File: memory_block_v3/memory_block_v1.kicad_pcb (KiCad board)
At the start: 4 copper layers, 69.6 x 49.6 mm, 15 parts, among them J1 4677, J11 Conn_01x07, J2 DM3D-SF, J3 Conn_01x02, J4 Conn_01x19, J5 Conn_01x03, J6 Conn_01x19, J7 PinSocket_1x03_P2.54mm_Vertic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, U1 ESP32-WROOM-32E-N4, U2 W25Q128JVSIQ TR

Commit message: Start of NB/MB PCB Rework
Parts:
- removed J7: PinSocket_1x03_P2.54mm_Vertical, Connector_PinSocket_2.54mm:PinSocket_1x03_P2.54mm_Vertical
- added C1: 10 uF, Capacitor_THT:CP_Radial_D10.0mm_P2.50mm, F.Cu at (342.1, 304.6)
- added C2: 0.1uF, Capacitor_THT:C_Rect_L7.5mm_W6.5mm_P5.00mm, F.Cu at (345.2, 292.9)
- added D1: LED, LED_THT:LED_D3.0mm, F.Cu at (337.8, 296.2)
- added R1: 220 Ω, Resistor_THT:R_Axial_DIN0207_L6.3mm_D2.5mm_P7.62mm_Horizontal, F.Cu at (337.8, 280.4)
- added R2: 10 kΩ, Resistor_THT:R_Axial_DIN0207_L6.3mm_D2.5mm_P7.62mm_Horizontal, F.Cu at (345.2, 280.4)
- U1: value ESP32-WROOM-32E-N4 -> ESP32-WROOM-32E-N8
- moved J5 90.1 mm to (378.7, 320.5)
- moved J11 82.4 mm to (378.7, 299.7)
- moved U1 54.8 mm to (362.2, 307.2)
- moved G*** 32.6 mm to (361.6, 295.6)
- moved H3 29.1 mm to (283.0, 339.0)
- moved J1 29.1 mm to (335.0, 313.4)
- moved H2 25.6 mm to (378.7, 288.6)
- moved H4 25.6 mm to (378.7, 332.8)
- moved J4 25.6 mm to (350.8, 287.7)
- moved J6 25.6 mm to (373.4, 287.6)
- moved J2 22.8 mm to (331.9, 327.9)
- moved U2 20.9 mm to (324.9, 313.1)
- moved H1 20.0 mm to (278.3, 263.7)
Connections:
- J1 pad 1: /HSPI_CS_PS -> /<NO NET>
- J1 pad 2: HSPI_MISO -> /<NO NET>
- J1 pad 5: HSPI_MOSI -> /<NO NET>
- J1 pad 6: HSPI_CLK -> /<NO NET>
- J1 pad 8: VCC -> /<NO NET>
- J2 pad 2: HSPI_CS_SD -> /<NO NET>
- J2 pad 3: HSPI_MOSI -> /<NO NET>
- J2 pad 4: VCC -> /<NO NET>
- J2 pad 5: HSPI_CLK -> /<NO NET>
- J2 pad 7: HSPI_MISO -> /<NO NET>
- J4 pad 10: unconnected-(J4-Pin_10-Pad10) -> /<NO NET>
- J4 pad 11: unconnected-(J4-Pin_11-Pad11) -> /<NO NET>
- J4 pad 12: unconnected-(J4-Pin_12-Pad12) -> HSPI_CLK
- J4 pad 13: unconnected-(J4-Pin_13-Pad13) -> HSPI_MISO
- J4 pad 15: unconnected-(J4-Pin_15-Pad15) -> HSPI_MOSI
- J4 pad 16: unconnected-(J4-Pin_16-Pad16) -> /<NO NET>
- J4 pad 17: unconnected-(J4-Pin_17-Pad17) -> /<NO NET>
- J4 pad 18: unconnected-(J4-Pin_18-Pad18) -> /<NO NET>
- J4 pad 19: unconnected-(J4-Pin_19-Pad19) -> 5V
- J4 pad 3: unconnected-(J4-Pin_3-Pad3) -> /<NO NET>
- J4 pad 4: unconnected-(J4-Pin_4-Pad4) -> /<NO NET>
- J4 pad 5: P_RX -> P_TX
- J4 pad 6: P_TX -> P_RX
- J4 pad 7: unconnected-(J4-Pin_7-Pad7) -> /<NO NET>
- J4 pad 8: unconnected-(J4-Pin_8-Pad8) -> /<NO NET>
- J4 pad 9: unconnected-(J4-Pin_9-Pad9) -> /<NO NET>
- J5 pad 1: /SB_TX -> SB_RX
- J5 pad 2: /SB_RX -> SB_TX
- J6 pad 10: /<NO NET> -> VSPI_CS
- J6 pad 11: /<NO NET> -> SB_RX
- J6 pad 12: /<NO NET> -> SB_TX
- J6 pad 13: /<NO NET> -> HSPI_CS_SD
- J6 pad 15: /<NO NET> -> HSPI_CS_PS
- J6 pad 16: /<NO NET> -> HSPI_CS_FL
- J6 pad 2: /<NO NET> -> VSPI_D0
- J6 pad 3: /<NO NET> -> VSPI_D3
- J6 pad 6: /<NO NET> -> VSPI_D2
- J6 pad 8: /<NO NET> -> VSPI_D1
- J6 pad 9: /<NO NET> -> VSPI_CLK
- U1 pad 23: /HSPI_CS_FL -> HSPI_CS_FL
- U1 pad 24: /HSPI_CS_PS -> HSPI_CS_PS
- U1 pad 27: unconnected-(U1-IO16-Pad27) -> SB_TX
- U1 pad 28: unconnected-(U1-IO17-Pad28) -> SB_RX
- U1 pad 34: P_RX -> unconnected-(U1-RXD0-Pad34)
- U1 pad 35: P_TX -> unconnected-(U1-TXD0-Pad35)
- U1 pad 6: /SB_TX -> P_TX
- U1 pad 7: /SB_RX -> P_RX
- U2 pad 1: /HSPI_CS_FL -> /<NO NET>
- U2 pad 2: HSPI_MISO -> /<NO NET>
- U2 pad 5: HSPI_MOSI -> /<NO NET>
- U2 pad 6: HSPI_CLK -> /<NO NET>
- U2 pad 8: VCC -> /<NO NET>
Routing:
- net HSPI_CLK: track 70.1 -> 3.28 mm, vias 4 -> 0
- net HSPI_MISO: track 67.8 -> 2.75 mm, vias 5 -> 0
- net HSPI_MOSI: track 58.1 -> 8.58 mm, vias 4 -> 0
- net BOOT: track 37.8 -> 3.38 mm
- net VSPI_D1: track 34.0 -> 6.82 mm, vias 2 -> 0
- net VSPI_CS: track 27.1 -> 0.00 mm, vias 2 -> 0
- net EN: track 34.9 -> 10.5 mm
- net VSPI_D2: track 35.0 -> 12.9 mm
- net /HSPI_CS_PS: track 21.7 -> 0.00 mm
- net P_TX: track 19.6 -> 0.00 mm
- net VSPI_CLK: track 26.5 -> 7.63 mm, vias 2 -> 0
- net HSPI_CS_SD: track 21.0 -> 2.86 mm
- net /HSPI_CS_FL: track 17.0 -> 0.00 mm
- net P_RX: track 14.8 -> 0.00 mm
- net SB_RX: track 0.00 -> 12.9 mm
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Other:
- board outline removed
- board text added: "${REFERENCE}"
- board text added: "ESP32-WROOM-32E"
- board text added: "RX TX GND"
- board text removed: "CLK MISO MOSI"
- board text removed: "HSPI Pinout"
- board text removed: "Programming Devkit"
- board text removed: "TX RX GND"

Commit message: continued NB/MB pcb progress
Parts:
- removed J11: Conn_01x07, Connector_PinSocket_2.54mm:PinSocket_1x07_P2.54mm_Vertical
- removed J5: Conn_01x03, Connector_PinSocket_2.54mm:PinSocket_1x03_P2.54mm_Vertical
- moved G*** 17.3 mm to (347.7, 305.9)
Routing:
- net SB_TX: track 12.3 -> 2.66 mm
- net SB_RX: track 12.9 -> 3.19 mm

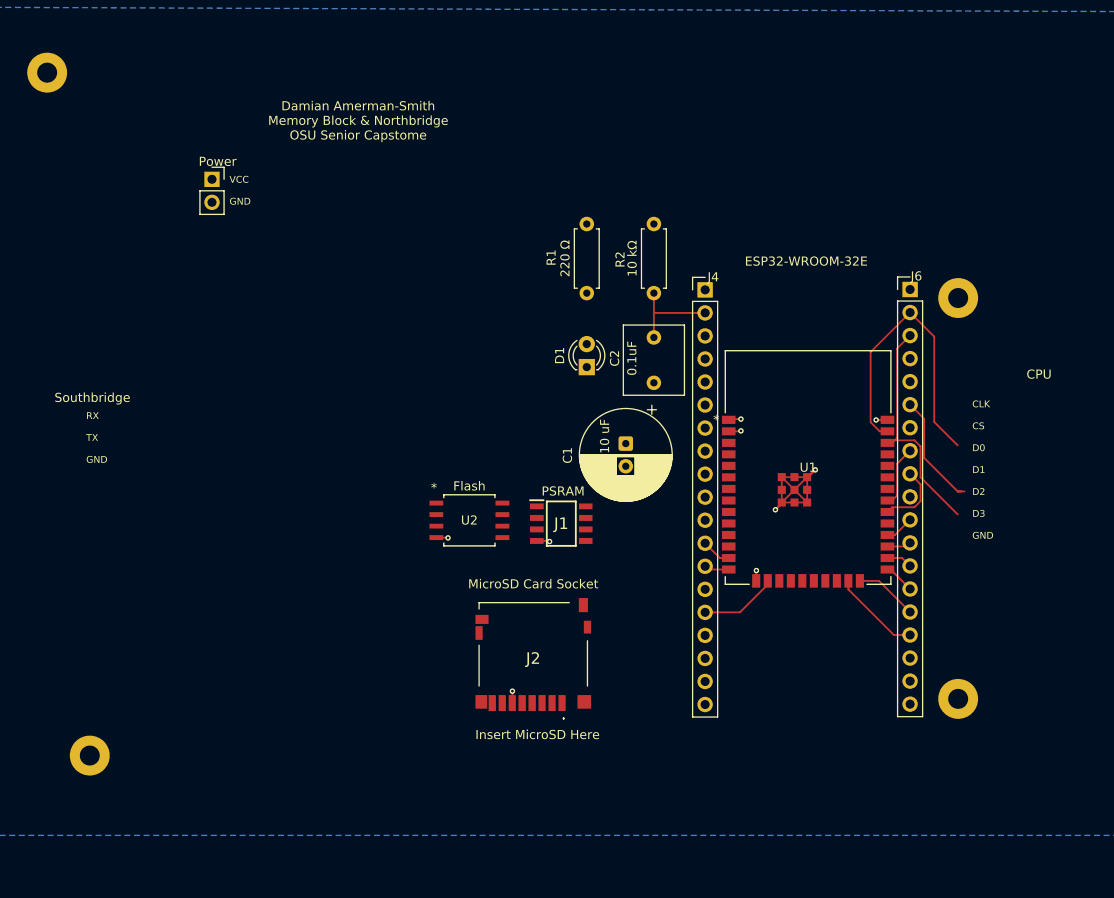
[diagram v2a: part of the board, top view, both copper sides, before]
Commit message: Changed header pins, redone PCB layout
Still need to do actual trace routing, but have general components mapped out.
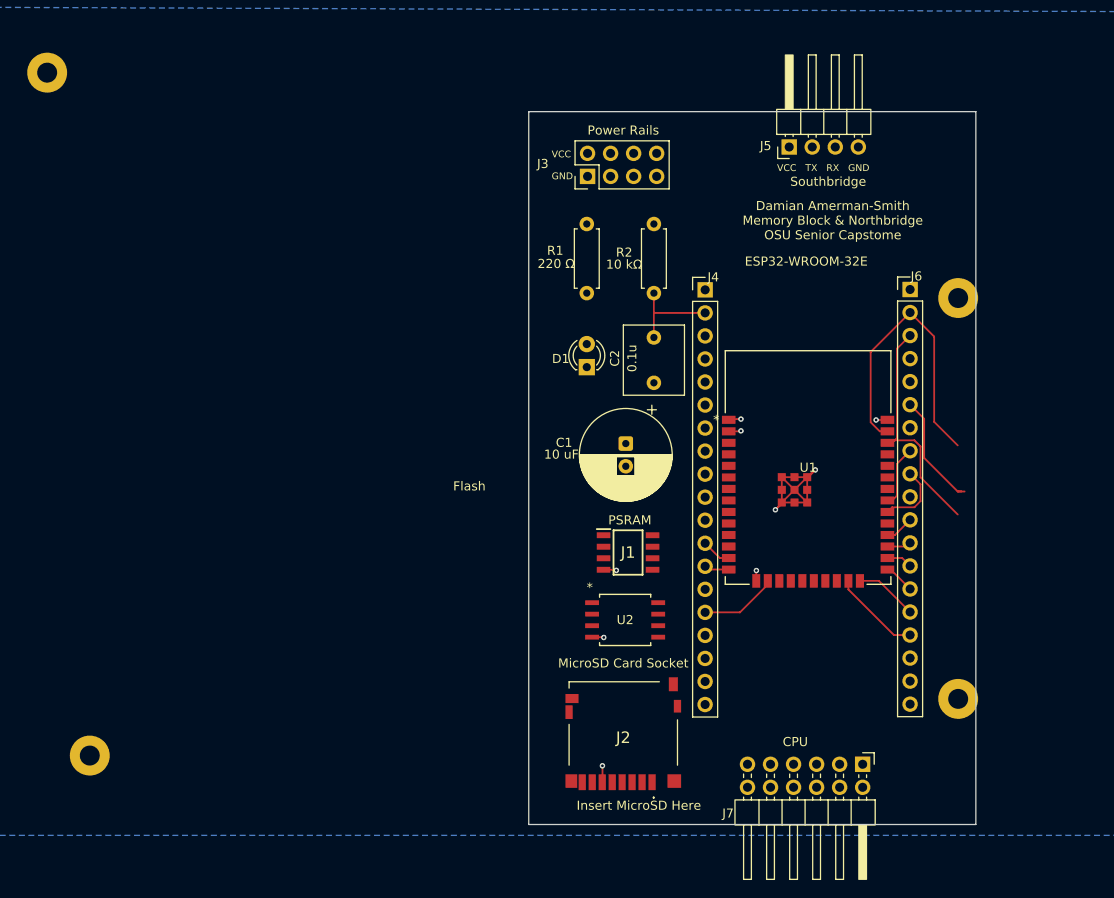
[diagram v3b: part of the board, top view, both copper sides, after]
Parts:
- added J5: Conn_01x04, Connector_PinHeader_2.54mm:PinHeader_1x04_P2.54mm_Horizontal, F.Cu at (360.1, 271.9)
- added J7: Conn_02x06_Top_Bottom, Connector_PinHeader_2.54mm:PinHeader_2x06_P2.54mm_Horizontal, F.Cu at (368.2, 340.0)
- C2: value 0.1uF -> 0.1u
- J3: value Conn_01x02 -> Conn_02x04_Odd_Even; footprint Connector_PinSocket_2.54mm:PinSocket_1x02_P2.54mm_Vertical -> Connector_PinHeader_2.54mm:PinHeader_2x04_P2.54mm_Vertical
- moved J3 41.4 mm to (337.9, 275.1), turned to 90 degrees
- moved G*** 40.5 mm to (375.0, 335.9)
- moved U2 20.4 mm to (342.0, 324.0)
- moved J2 13.2 mm to (341.8, 336.6)
- moved J1 8.02 mm to (342.4, 316.6)
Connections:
- C1 pad 1: VCC -> /<NO NET>
- C2 pad 1: EN -> /<NO NET>
- J3 pad 1: VCC -> GND
- J3 pad 2: GND -> VCC
- J4 pad 1: VCC -> /<NO NET>
- J4 pad 12: HSPI_CLK -> /<NO NET>
- J4 pad 13: HSPI_MISO -> /<NO NET>
- J4 pad 15: HSPI_MOSI -> /<NO NET>
- J4 pad 19: 5V -> /<NO NET>
- J4 pad 2: EN -> /<NO NET>
- J4 pad 5: P_TX -> /<NO NET>
- J4 pad 6: P_RX -> /<NO NET>
- J6 pad 10: VSPI_CS -> /<NO NET>
- J6 pad 11: SB_RX -> /<NO NET>
- J6 pad 12: SB_TX -> /<NO NET>
- J6 pad 13: HSPI_CS_SD -> /<NO NET>
- J6 pad 14: BOOT -> /<NO NET>
- J6 pad 15: HSPI_CS_PS -> /<NO NET>
- J6 pad 16: HSPI_CS_FL -> /<NO NET>
- J6 pad 2: VSPI_D0 -> /<NO NET>
- J6 pad 3: VSPI_D3 -> /<NO NET>
- J6 pad 6: VSPI_D2 -> /<NO NET>
- J6 pad 8: VSPI_D1 -> /<NO NET>
- J6 pad 9: VSPI_CLK -> /<NO NET>
- R2 pad 1: VCC -> /<NO NET>
- R2 pad 2: EN -> /<NO NET>
- U1 pad 11: unconnected-(U1-IO26-Pad11) -> /<NO NET>
- U1 pad 12: unconnected-(U1-IO27-Pad12) -> /<NO NET>
- U1 pad 13: HSPI_CLK -> /<NO NET>
- U1 pad 14: HSPI_MISO -> /<NO NET>
- U1 pad 16: HSPI_MOSI -> /<NO NET>
- U1 pad 2: VCC -> /<NO NET>
- U1 pad 23: HSPI_CS_FL -> /<NO NET>
- U1 pad 24: HSPI_CS_PS -> /<NO NET>
- U1 pad 25: BOOT -> /<NO NET>
- U1 pad 26: HSPI_CS_SD -> /<NO NET>
- U1 pad 27: SB_TX -> /<NO NET>
- U1 pad 28: SB_RX -> /<NO NET>
- U1 pad 29: VSPI_CS -> /<NO NET>
- U1 pad 3: EN -> /<NO NET>
- U1 pad 30: VSPI_CLK -> /<NO NET>
- U1 pad 31: VSPI_D1 -> /<NO NET>
- U1 pad 33: VSPI_D2 -> /<NO NET>
- U1 pad 36: VSPI_D3 -> /<NO NET>
- U1 pad 37: VSPI_D0 -> /<NO NET>
- U1 pad 6: P_TX -> /<NO NET>
- U1 pad 7: P_RX -> /<NO NET>
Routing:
- net /<NO NET>: track 0.33 -> 143.0 mm, vias 0 -> 1
- net VSPI_D0: track 33.5 -> 0.00 mm
- net VSPI_D3: track 26.4 -> 0.00 mm
- net VSPI_D2: track 12.9 -> 0.00 mm
- net EN: track 10.5 -> 0.00 mm
- net HSPI_CS_FL: track 9.83 -> 0.00 mm
- net HSPI_MOSI: track 8.58 -> 0.00 mm
- net VSPI_CLK: track 7.63 -> 0.00 mm
- net HSPI_CS_PS: track 6.95 -> 0.00 mm
- net VSPI_D1: track 6.82 -> 0.00 mm
- net BOOT: track 3.38 -> 0.00 mm
- net HSPI_CLK: track 3.28 -> 0.00 mm
- net SB_RX: track 3.19 -> 0.00 mm
- net HSPI_CS_SD: track 2.86 -> 0.00 mm
- net HSPI_MISO: track 2.75 -> 0.00 mm
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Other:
- board outline added: 49.3 x 78.6 mm
- board text added: "Power Rails"
- board text added: "VCC TX RX GND"
- board text removed: "CLK CS D0 D1 D2 D3 GND"
- board text removed: "Power"
- board text removed: "RX TX GND"

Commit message: Continued PCB Layout Edits
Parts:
- C1: value 10 uF -> 470 uF
- C2: value 0.1u -> 0.1 μF
- moved H1 57.8 mm to (334.8, 275.8)
- moved H3 52.1 mm to (334.9, 342.7)
- moved G*** 32.3 mm to (393.0, 309.0)
- moved R1 31.4 mm to (345.7, 310.8)
- moved J2 21.2 mm to (363.0, 337.3)
- moved D1 17.9 mm to (338.1, 314.0), turned to -90 degrees
- moved J7 15.1 mm to (353.1, 339.9)
- moved H2 13.0 mm to (376.2, 275.8)
- moved H4 10.3 mm to (376.0, 342.7)
- moved U2 8.07 mm to (341.5, 332.1)
- moved J1 7.46 mm to (341.0, 324.0)
- moved J3 5.86 mm to (342.9, 278.2)
- moved J5 4.01 mm to (360.6, 275.9)
- moved C1 1.91 mm to (342.2, 302.7)
- moved C2 1.47 mm to (345.2, 291.4)
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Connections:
- C1 pad 1: /<NO NET> -> VCC
- C2 pad 1: /<NO NET> -> EN
- J1 pad 1: /<NO NET> -> HSPI_CS_PS
- J1 pad 2: /<NO NET> -> HSPI_MISO
- J1 pad 5: /<NO NET> -> HSPI_MOSI
- J1 pad 6: /<NO NET> -> HSPI_CLK
- J1 pad 8: /<NO NET> -> VCC
- J2 pad 2: /<NO NET> -> HSPI_CS_SD
- J2 pad 3: /<NO NET> -> HSPI_MOSI
- J2 pad 4: /<NO NET> -> VCC
- J2 pad 5: /<NO NET> -> HSPI_CLK
- J2 pad 7: /<NO NET> -> HSPI_MISO
- J4 pad 1: /<NO NET> -> VCC
- J4 pad 10: /<NO NET> -> CPU_IO0
- J4 pad 11: /<NO NET> -> CPU_IO1
- J4 pad 12: /<NO NET> -> HSPI_CLK
- J4 pad 13: /<NO NET> -> HSPI_MISO
- J4 pad 15: /<NO NET> -> HSPI_MOSI
- J4 pad 2: /<NO NET> -> EN
- J4 pad 5: /<NO NET> -> P_TX
- J4 pad 6: /<NO NET> -> P_RX
- J6 pad 10: /<NO NET> -> VSPI_CS
- J6 pad 11: /<NO NET> -> SB_RX
- J6 pad 12: /<NO NET> -> SB_TX
- J6 pad 13: /<NO NET> -> HSPI_CS_SD
- J6 pad 2: /<NO NET> -> VSPI_D0
- J6 pad 3: /<NO NET> -> VSPI_D3
- J6 pad 6: /<NO NET> -> VSPI_D2
- J6 pad 8: /<NO NET> -> VSPI_D1
- J6 pad 9: /<NO NET> -> VSPI_CLK
- R2 pad 1: /<NO NET> -> VCC
- R2 pad 2: /<NO NET> -> EN
- U1 pad 11: /<NO NET> -> CPU_IO0
- U1 pad 12: /<NO NET> -> CPU_IO1
- U1 pad 13: /<NO NET> -> HSPI_CLK
- U1 pad 14: /<NO NET> -> HSPI_MISO
- U1 pad 16: /<NO NET> -> HSPI_MOSI
- U1 pad 2: /<NO NET> -> VCC
- U1 pad 23: /<NO NET> -> HSPI_CS_FL
- U1 pad 24: /<NO NET> -> HSPI_CS_PS
- U1 pad 25: /<NO NET> -> BOOT
- U1 pad 26: /<NO NET> -> HSPI_CS_SD
- U1 pad 27: /<NO NET> -> SB_TX
- U1 pad 28: /<NO NET> -> SB_RX
- U1 pad 29: /<NO NET> -> VSPI_CS
- U1 pad 3: /<NO NET> -> EN
- U1 pad 30: /<NO NET> -> VSPI_CLK
- U1 pad 31: /<NO NET> -> VSPI_D1
- U1 pad 33: /<NO NET> -> VSPI_D2
- U1 pad 36: /<NO NET> -> VSPI_D3
- U1 pad 37: /<NO NET> -> VSPI_D0
- U1 pad 6: /<NO NET> -> P_TX
- U1 pad 7: /<NO NET> -> P_RX
- U2 pad 1: /<NO NET> -> HSPI_CS_FL
- U2 pad 2: /<NO NET> -> HSPI_MISO
- U2 pad 5: /<NO NET> -> HSPI_MOSI
- U2 pad 6: /<NO NET> -> HSPI_CLK
- U2 pad 8: /<NO NET> -> VCC
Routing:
- net /<NO NET>: track 143.0 -> 20.2 mm
- net VSPI_D0: track 0.00 -> 16.6 mm
- net VSPI_D3: track 0.00 -> 13.6 mm
- net HSPI_MOSI: track 0.00 -> 8.58 mm
- net Net-(D1-A): track 0.00 -> 8.35 mm
- net EN: track 0.00 -> 8.18 mm
- net VSPI_CLK: track 0.00 -> 7.63 mm
- net VSPI_D1: track 0.00 -> 6.82 mm
- net HSPI_CLK: track 0.00 -> 3.28 mm
- net SB_RX: track 0.00 -> 3.19 mm
- net HSPI_CS_SD: track 0.00 -> 2.86 mm
- net HSPI_MISO: track 0.00 -> 2.75 mm
- net SB_TX: track 0.00 -> 2.66 mm
- net VCC: track 0.00 -> 1.37 mm
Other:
- board size 49.3 x 78.6 mm -> 48.5 x 74.2 mm
- board text added: "Damian Amerman-Smith Memory Block & Northbridge OSU Senior Capstone"
- board text removed: "Damian Amerman-Smith Memory Block & Northbridge OSU Senior Capstome"

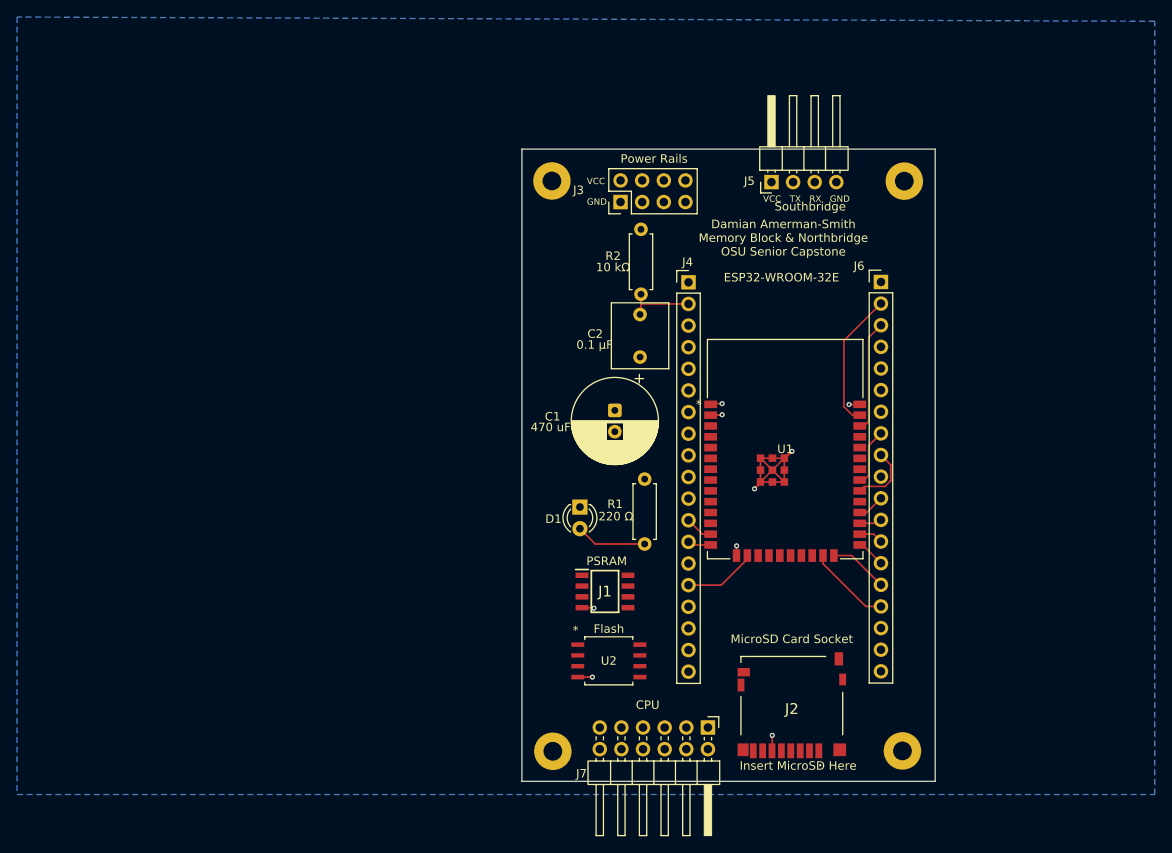
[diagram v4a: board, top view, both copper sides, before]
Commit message: First Draft of Signal Routing
Need to length-match SPI traces and perhaps simplify how signals cross over each other. Also, next goal is decoration.
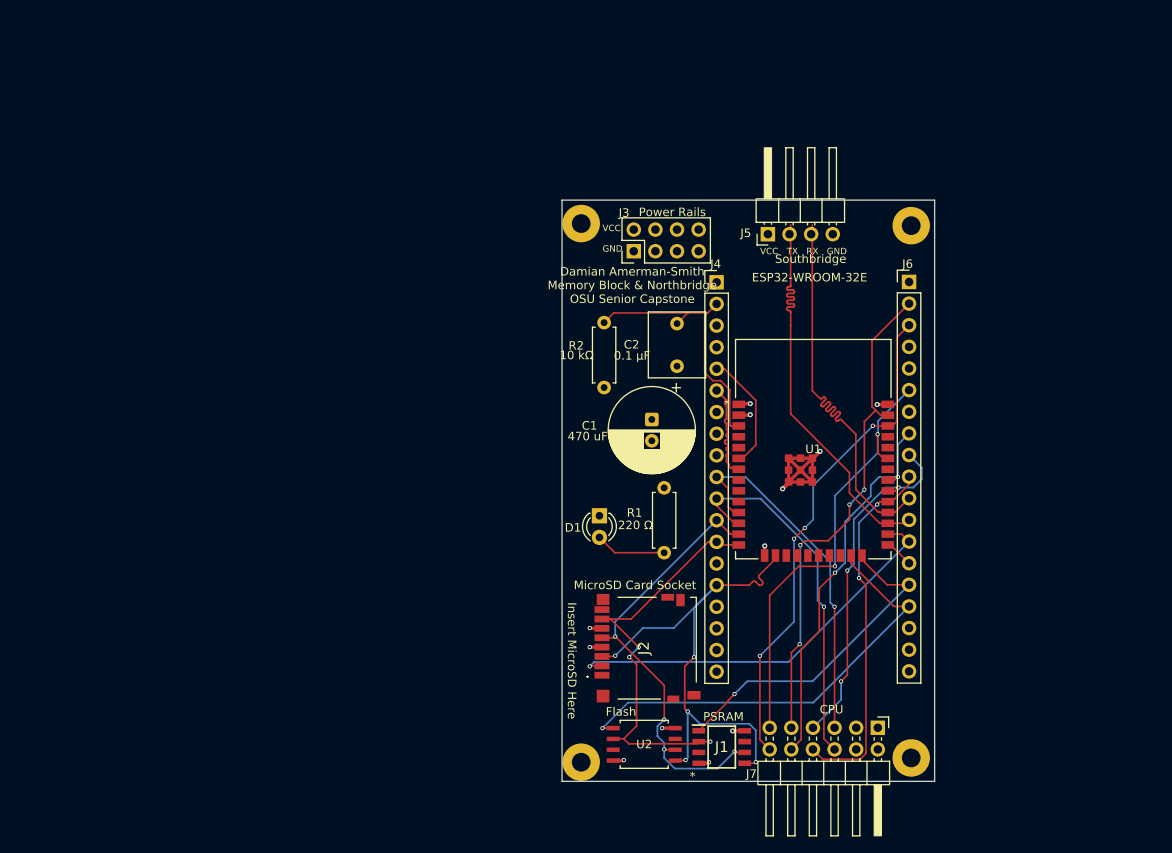
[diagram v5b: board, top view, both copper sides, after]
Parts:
- moved G*** 80.8 mm to (318.8, 341.0), turned to 90 degrees
- moved J1 22.8 mm to (354.8, 342.2)
- moved J7 20.0 mm to (373.1, 340.0)
- moved R2 19.1 mm to (340.9, 300.0), turned to 90 degrees
- moved J2 18.2 mm to (346.0, 330.6), turned to -90 degrees
- moved U2 10.6 mm to (345.6, 341.9)
- moved J5 6.13 mm to (360.2, 282.0)
- moved H1 6.07 mm to (338.2, 280.8)
- moved J3 5.98 mm to (344.4, 284.0)
- moved H2 5.29 mm to (377.0, 281.0)
- moved C1 4.47 mm to (346.5, 303.8)
- moved C2 4.47 mm to (349.5, 292.5)
- moved H3 3.57 mm to (338.2, 344.0)
- moved J4 3.30 mm to (354.1, 287.7)
- moved J6 3.30 mm to (376.7, 287.6)
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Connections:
- J6 pad 14: /<NO NET> -> BOOT
- J6 pad 15: /<NO NET> -> HSPI_CS_PS
- J6 pad 16: /<NO NET> -> HSPI_CS_FL
- J7 pad 10: /<NO NET> -> VSPI_D1
- J7 pad 11: /<NO NET> -> VSPI_D2
- J7 pad 12: /<NO NET> -> VSPI_D3
- J7 pad 5: /<NO NET> -> CPU_IO0
- J7 pad 6: /<NO NET> -> CPU_IO1
- J7 pad 7: /<NO NET> -> VSPI_CLK
- J7 pad 8: /<NO NET> -> VSPI_CS
- J7 pad 9: /<NO NET> -> VSPI_D0
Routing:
- net HSPI_MOSI: track 8.58 -> 64.6 mm, vias 0 -> 5
- net HSPI_CS_FL: track 0.33 -> 53.0 mm, vias 0 -> 1
- net VSPI_D2: track 0.00 -> 52.6 mm, vias 0 -> 2
- net HSPI_CLK: track 3.28 -> 52.9 mm, vias 0 -> 4
- net HSPI_MISO: track 2.75 -> 49.9 mm, vias 0 -> 3
- net SB_TX: track 2.66 -> 48.1 mm
- net VSPI_D3: track 13.6 -> 58.9 mm, vias 0 -> 4
- net HSPI_CS_SD: track 2.86 -> 47.9 mm, vias 0 -> 1
- net SB_RX: track 3.19 -> 47.9 mm
- net VSPI_CS: track 0.00 -> 43.1 mm, vias 0 -> 2
- net CPU_IO0: track 0.00 -> 42.8 mm, vias 0 -> 1
- net VSPI_D0: track 16.6 -> 59.2 mm, vias 0 -> 4
- net CPU_IO1: track 0.00 -> 42.5 mm, vias 0 -> 1
- net HSPI_CS_PS: track 0.00 -> 39.1 mm, vias 0 -> 1
- net VSPI_D1: track 6.82 -> 45.5 mm, vias 0 -> 2
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- added copper zone on In2.Cu, net GND
- removed copper zone on B.Cu, net GND
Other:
- board size 48.5 x 74.2 mm -> 43.8 x 68.2 mm
